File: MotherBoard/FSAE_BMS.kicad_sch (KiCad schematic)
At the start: 0 parts

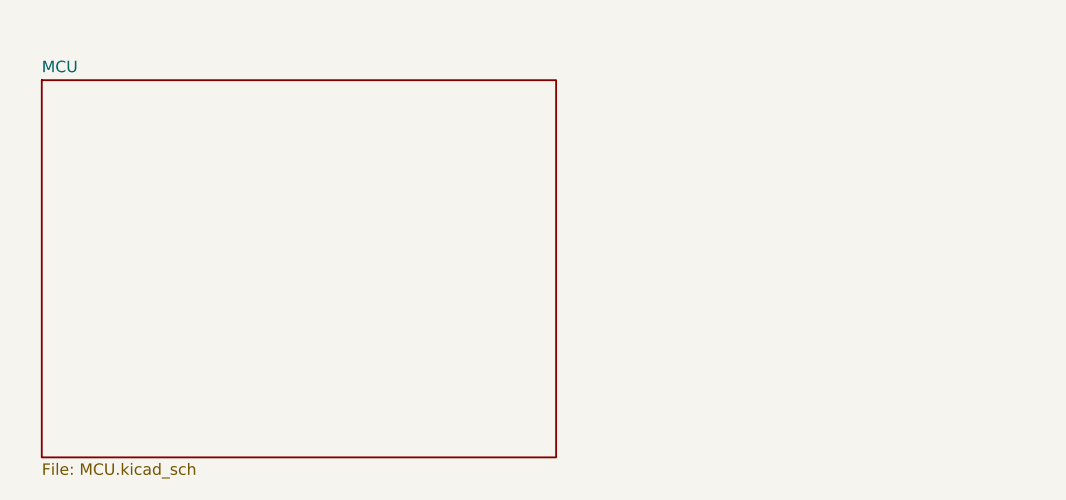
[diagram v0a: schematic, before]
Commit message: Added IO Connector and uC
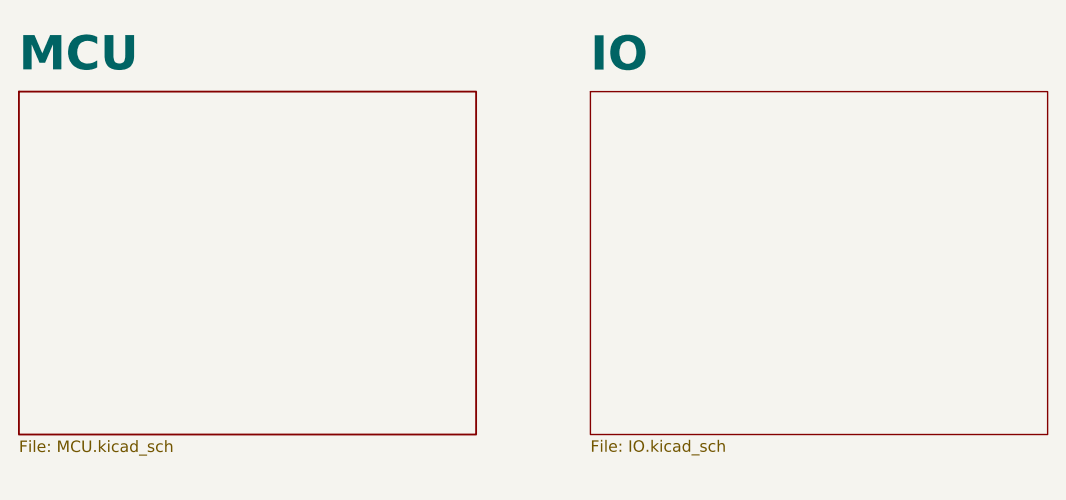
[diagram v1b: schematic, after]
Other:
- added sheet IO (IO.kicad_sch)
- company: (none) -> FSAE LSU
- title: (none) -> STM32 Layout
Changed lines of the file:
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@@
 	(generator_version "8.0")
 	(paper "A4")
+	(title_block
+		(title "STM32 Layout")
+		(date "2024-10-15")
+		(rev "A")
+		(company "FSAE LSU")
+	)
 	(sheet
-		(at 40.64 36.83)
-		(size 57.15 41.91)
+		(at 38.1 38.1)
+		(size 50.8 38.1)
 		(fields_autoplaced yes)
 		(stroke
@@
 		)
 		(property "Sheetname" "MCU"
-			(at 40.64 36.093 0)
+			(at 38.1 36.093 0)
 			(effects
 				(font
-					(size 1.27 1.27)
+					(size 3.81 3.81)
+					(bold yes)
 				)
 				(justify left bottom)
@@
 		)
 		(property "Sheetfile" "MCU.kicad_sch"
-			(at 40.64 79.35 0)
+			(at 38.1 76.81 0)
 			(effects
 				(font
@@
 				)
 			)
+		)
+	)
+	(sheet
+		(at 101.6 38.1)
+		(size 50.8 38.1)
+		(fields_autoplaced yes)
+		(stroke
+			(width 0.1524)
+			(type solid)
+		)
+		(fill
+			(color 0 0 0 0.0000)
+		)
+		(property "Sheetname" "IO"
+			(at 101.6 36.1184 0)
+			(effects
+				(font
+					(size 3.81 3.81)
+					(bold yes)
+				)
+				(justify left bottom)
+			)
+		)
+		(property "Sheetfile" "IO.kicad_sch"
+			(at 101.6 76.7846 0)
+			(effects
+				(font
+					(size 1.27 1.27)
+				)
+				(justify left top)
+			)
+		)
+		(instances
+			(project "FSAE_BMS"
+				(path "/335e81e9-b957-4266-8116-dde74329bfca"
+					(page "3")
+				)
+			)

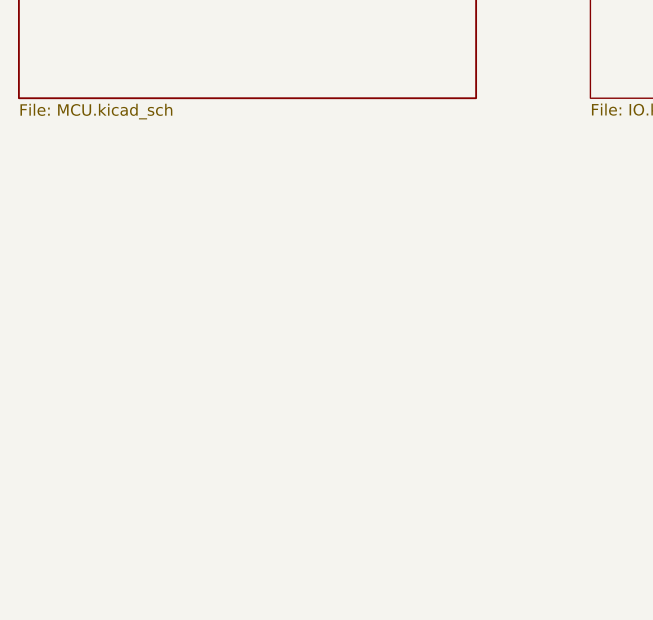
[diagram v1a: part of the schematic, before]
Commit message: Complete bootstrap schematic for MCU
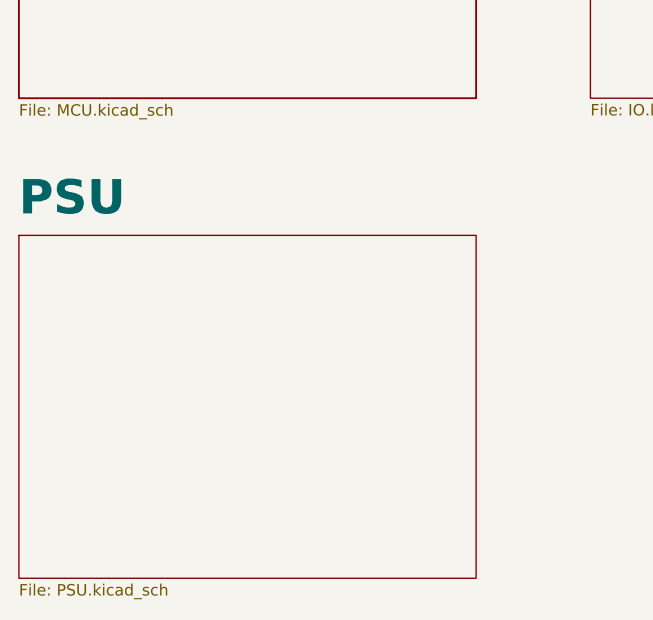
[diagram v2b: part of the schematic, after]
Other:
- added sheet PSU (PSU.kicad_sch)
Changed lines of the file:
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@@
 		(rev "A")
 		(company "FSAE LSU")
+		(comment 1 "Jacob Parent ")
+		(comment 2 "parent.jacob7@protonmail.com")
 	)
 	(sheet
@@
 				)
 			)
+		)
+	)
+	(sheet
+		(at 38.1 91.44)
+		(size 50.8 38.1)
+		(fields_autoplaced yes)
+		(stroke
+			(width 0.1524)
+			(type solid)
+		)
+		(fill
+			(color 0 0 0 0.0000)
+		)
+		(property "Sheetname" "PSU"
+			(at 38.1 89.4584 0)
+			(effects
+				(font
+					(size 3.81 3.81)
+					(bold yes)
+				)
+				(justify left bottom)
+			)
+		)
+		(property "Sheetfile" "PSU.kicad_sch"
+			(at 38.1 130.1246 0)
+			(effects
+				(font
+					(size 1.27 1.27)
+				)
+				(justify left top)
+			)
+		)
+		(instances
+			(project "FSAE_BMS"
+				(path "/335e81e9-b957-4266-8116-dde74329bfca"
+					(page "4")
+				)
+			)

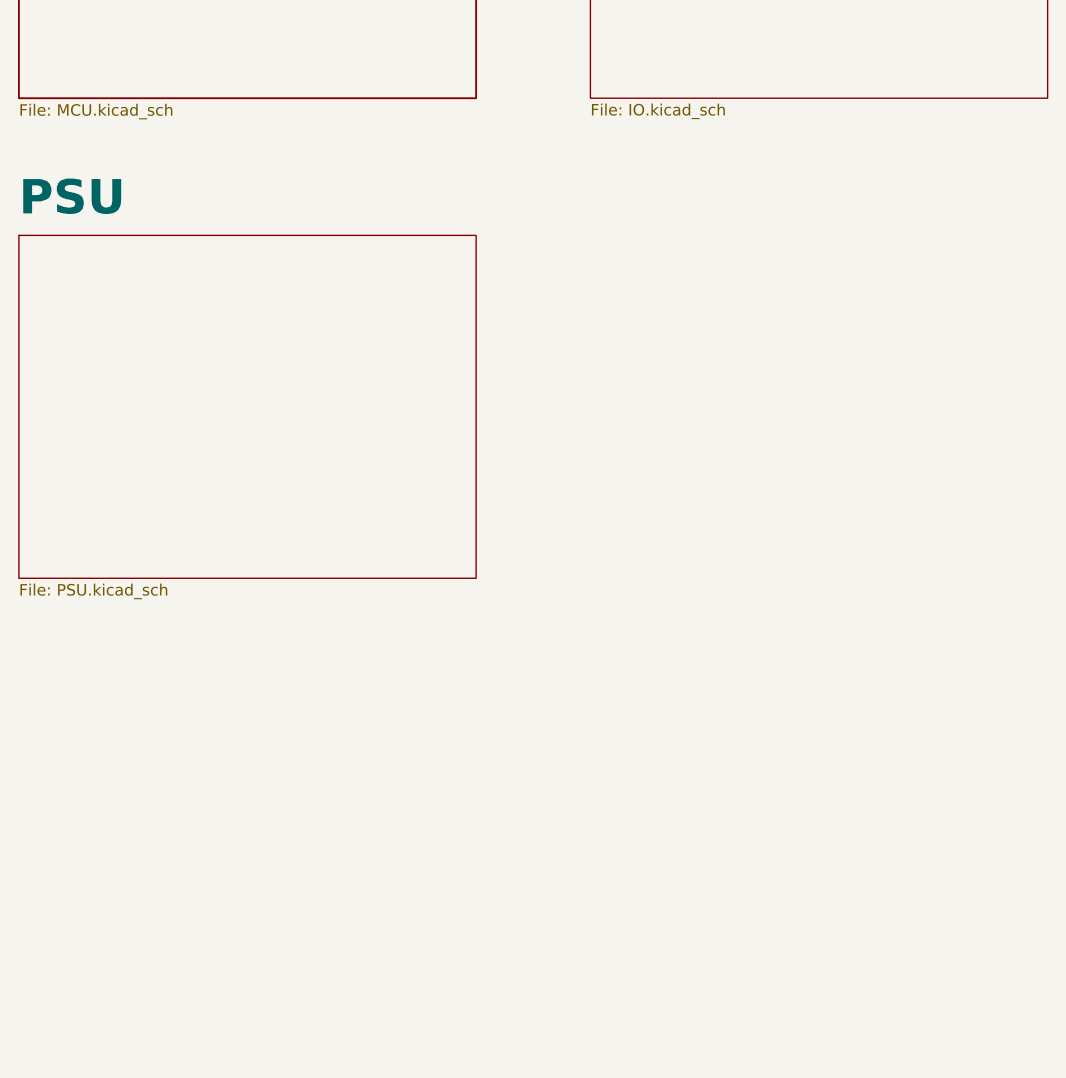
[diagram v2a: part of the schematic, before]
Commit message: Added BQ7900 rough draft and TCAN
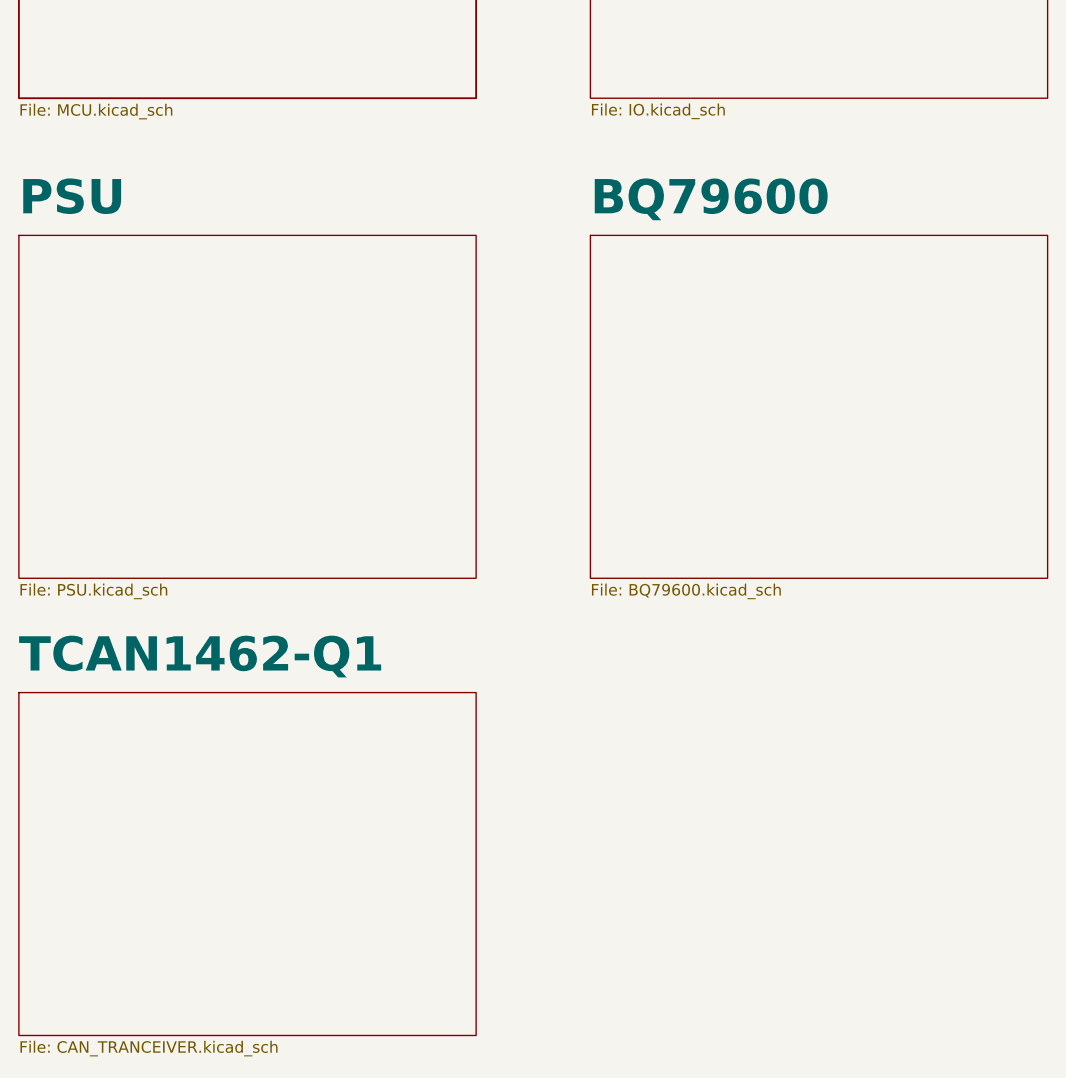
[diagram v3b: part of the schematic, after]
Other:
- added sheet BQ79600 (BQ79600.kicad_sch)
- added sheet TCAN1462-Q1 (CAN_TRANCEIVER.kicad_sch)
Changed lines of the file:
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@@
+	)
+	(sheet
+		(at 38.1 142.24)
+		(size 50.8 38.1)
+		(fields_autoplaced yes)
+		(stroke
+			(width 0.1524)
+			(type solid)
+		)
+		(fill
+			(color 0 0 0 0.0000)
+		)
+		(property "Sheetname" "TCAN1462-Q1"
+			(at 38.1 140.2584 0)
+			(effects
+				(font
+					(size 3.81 3.81)
+					(bold yes)
+				)
+				(justify left bottom)
+			)
+		)
+		(property "Sheetfile" "CAN_TRANCEIVER.kicad_sch"
+			(at 38.1 180.9246 0)
+			(effects
+				(font
+					(size 1.27 1.27)
+				)
+				(justify left top)
+			)
+		)
+		(instances
+			(project "FSAE_BMS"
+				(path "/335e81e9-b957-4266-8116-dde74329bfca"
+					(page "6")
+				)
+			)
+		)
 	)
 	(sheet
@@
 				)
 			)
+		)
+	)
+	(sheet
+		(at 101.6 91.44)
+		(size 50.8 38.1)
+		(fields_autoplaced yes)
+		(stroke
+			(width 0.1524)
+			(type solid)
+		)
+		(fill
+			(color 0 0 0 0.0000)
+		)
+		(property "Sheetname" "BQ79600"
+			(at 101.6 89.4584 0)
+			(effects
+				(font
+					(size 3.81 3.81)
+					(bold yes)
+				)
+				(justify left bottom)
+			)
+		)
+		(property "Sheetfile" "BQ79600.kicad_sch"
+			(at 101.6 130.1246 0)
+			(effects
+				(font
+					(size 1.27 1.27)
+				)
+				(justify left top)
+			)
+		)
+		(instances
+			(project "FSAE_BMS"
+				(path "/335e81e9-b957-4266-8116-dde74329bfca"
+					(page "5")
+				)
+			)

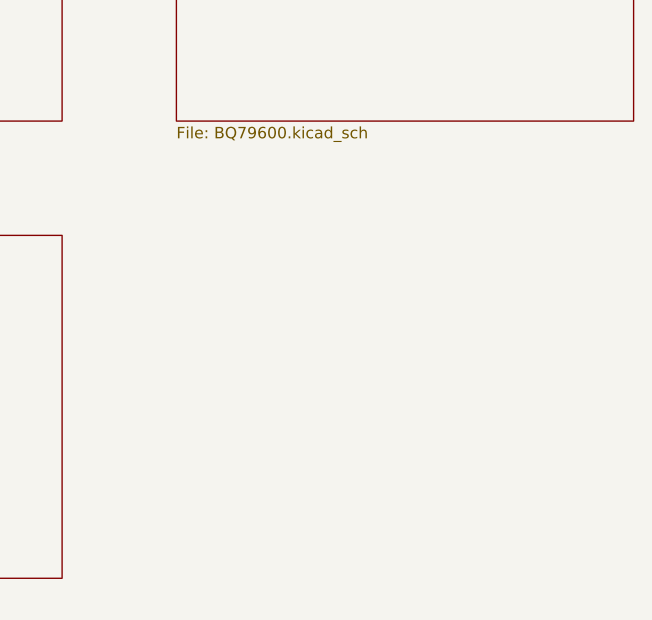
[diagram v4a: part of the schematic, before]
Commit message: Fixed CAN tranceivers + added relay driver circuit + fixed relative file paths for 3D models + finished PSU but still need correct 3D model
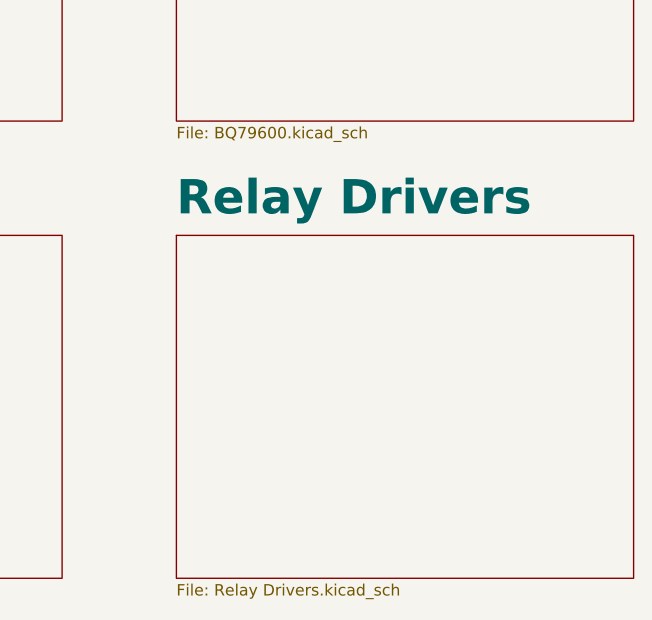
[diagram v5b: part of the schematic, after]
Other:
- added sheet Relay Drivers (Relay Drivers.kicad_sch)
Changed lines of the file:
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@@
+	)
+	(sheet
+		(at 101.6 142.24)
+		(size 50.8 38.1)
+		(fields_autoplaced yes)
+		(stroke
+			(width 0.1524)
+			(type solid)
+		)
+		(fill
+			(color 0 0 0 0.0000)
+		)
+		(property "Sheetname" "Relay Drivers"
+			(at 101.6 140.2584 0)
+			(effects
+				(font
+					(size 3.81 3.81)
+					(thickness 0.762)
+					(bold yes)
+				)
+				(justify left bottom)
+			)
+		)
+		(property "Sheetfile" "Relay Drivers.kicad_sch"
+			(at 101.6 180.9246 0)
+			(effects
+				(font
+					(size 1.27 1.27)
+				)
+				(justify left top)
+			)
+		)
+		(instances
+			(project "FSAE_BMS"
+				(path "/335e81e9-b957-4266-8116-dde74329bfca"
+					(page "7")
+				)
+			)
+		)
 	)
 	(sheet

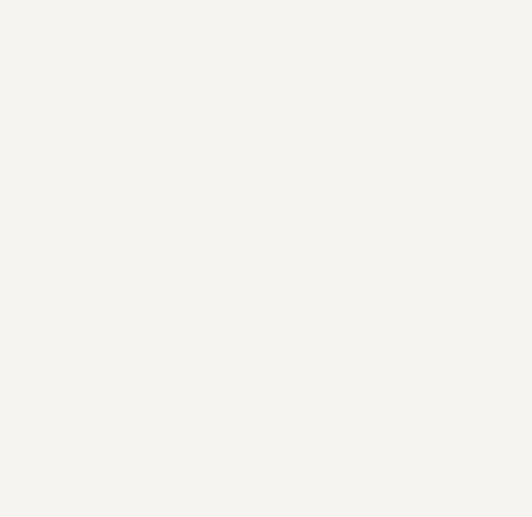
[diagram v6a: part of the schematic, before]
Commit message: Fixed relative paths + 90% footprints done + organized PCB for layout + found JLC part #s for manufacturing
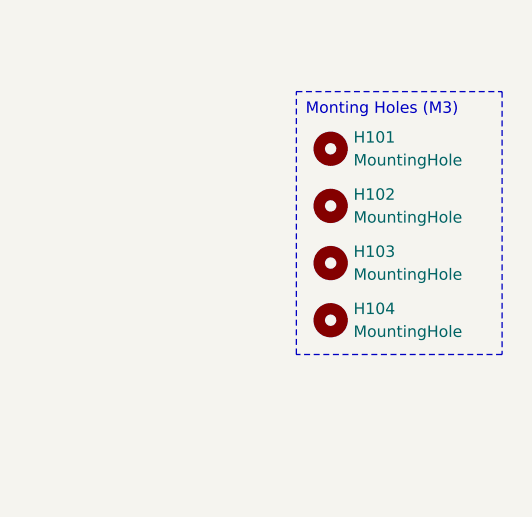
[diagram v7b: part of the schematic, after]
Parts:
- added H101, H102, H103, H104: MountingHole, MountingHole:MountingHole_3.2mm_M3, symbol Mechanical:MountingHole
